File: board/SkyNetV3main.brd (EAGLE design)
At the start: 38 x 67 mm, 61 parts, among them IC1 HC_05, IC2 RF4463PRO, IC3 LPC1769, IC4 BCX17, IC5 TPS63001, IC6 MCP73871-2CCI/ML, Q1 32.768KHz, Q2 12MHz, Q3 IRLM6402, Q4 BSS138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

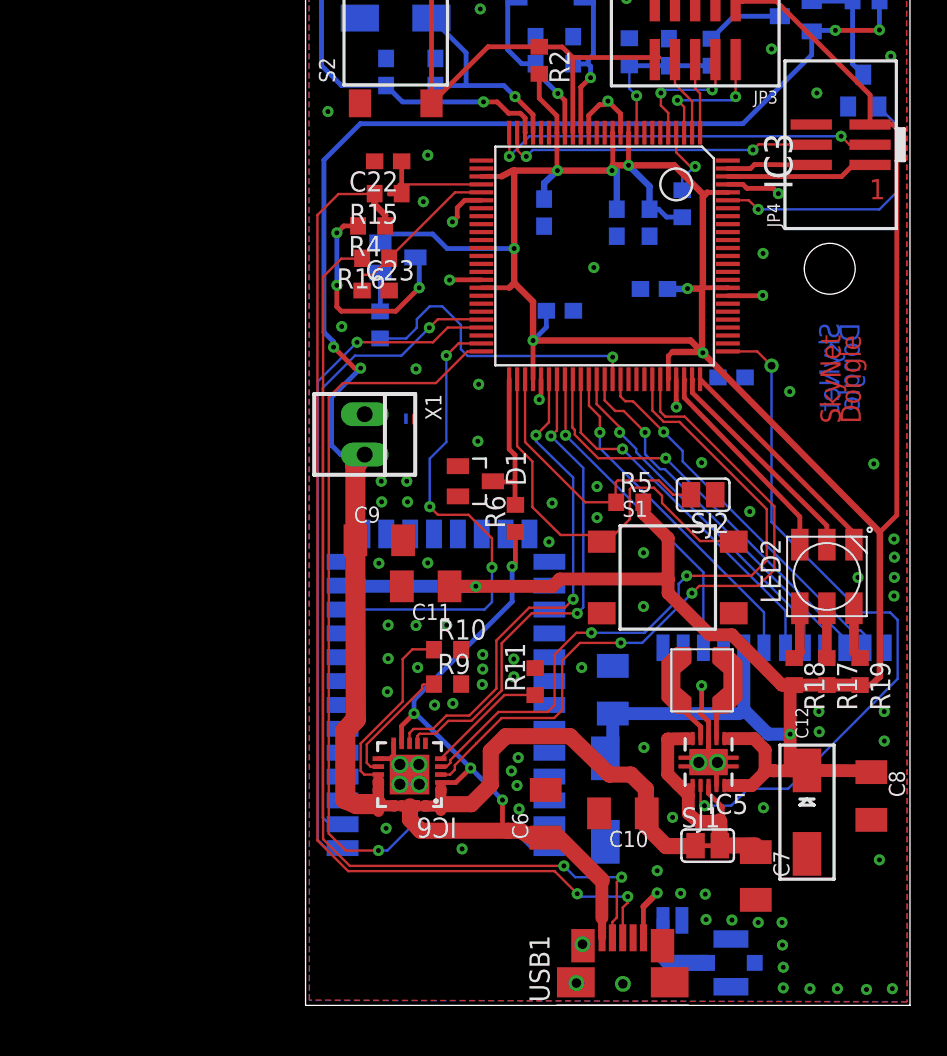
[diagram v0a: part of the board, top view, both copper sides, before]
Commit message: Schematic revised. TODO Radio remains
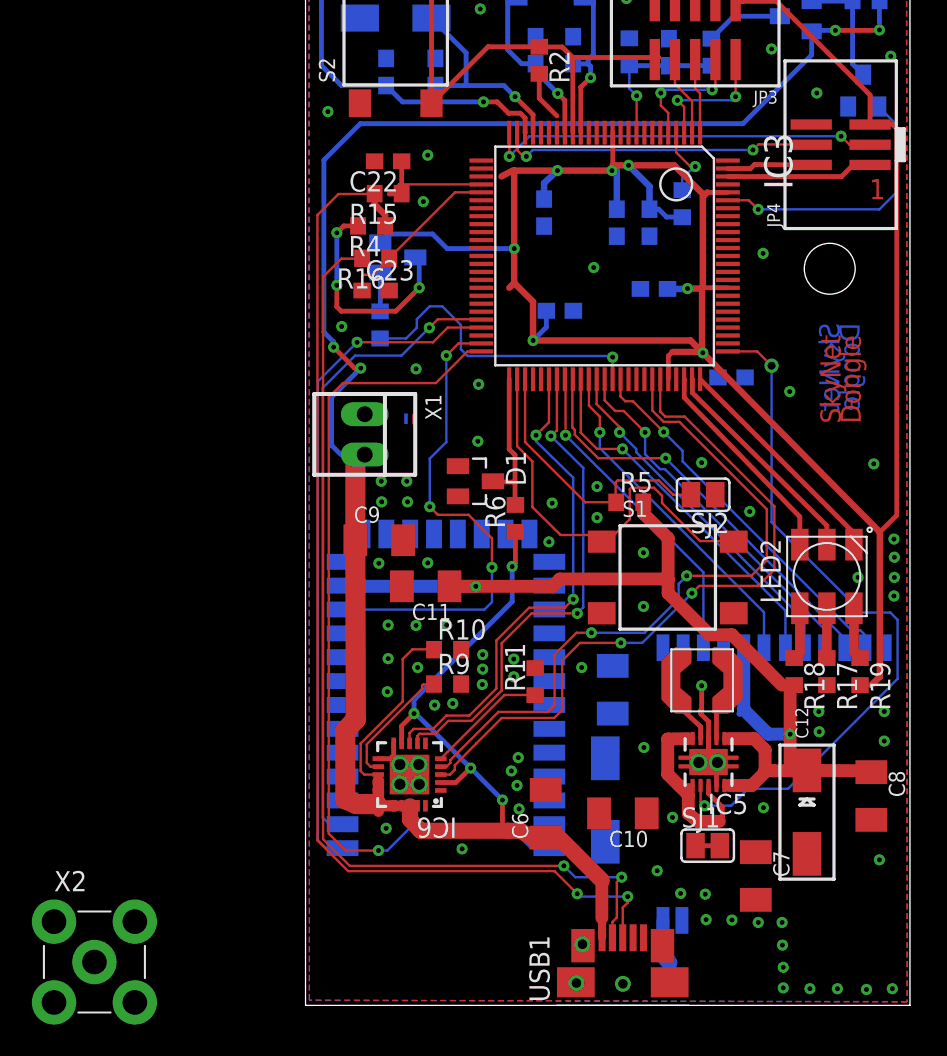
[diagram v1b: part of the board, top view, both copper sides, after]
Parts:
- removed U$1: ANT-MML, skynet_other:MML-2.0
- added X2: CONN-SMATHD, SteveMarple:SMA-THD
- R3: value 50 -> 1k
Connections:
- removed net OUT2: C10.1, IC6.1, IC6.20, SJ1.1
- new net BT-CN: IC1.32, IC3.48
- new net N$2: SJ1.1, X1.2
- net ANT: now also X2.SIG; no longer U$1.ANT
- net GND: now also IC1.21, IC1.22, X2.GND@0, X2.GND@1, X2.GND@2, X2.GND@3; no longer U$1.GND$1, U$1.GND$2, U$1.GND$3
- net V+: now also SJ1.2; no longer X1.2
- net VCC: now also C10.1, IC6.1, IC6.20; no longer SJ1.2
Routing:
- net OUT2: track 28.1 -> 0.00 mm
- net +3V3: track 244.3 -> 217.2 mm
- net GND: track 33.1 -> 11.5 mm, vias 96 -> 88
- net VCC: track 16.7 -> 13.0 mm
- net V+: track 93.7 -> 91.3 mm
- net ANT: track 5.19 -> 2.82 mm

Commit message: Schematic revised
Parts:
- removed X1: BAT, con-molex:22-23-2021
- added B1: PL503465, i7:PL503465
- added C14, C24: 10u, rcl:C1206K
- added Q5, Q6: IRLM6402, microbuilder:SOT23-WIDE
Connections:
- new net /BT-ON: IC3.32
- new net /RF-ON: IC3.33
- new net N$3: Q5.1
- new net N$4: Q6.1
- new net VDD: C11.1, IC1.12, Q5.3
- new net VEE: C1.1, C13.+, IC2.VCC, Q6.3
- net +3V3: now also C14.1, Q5.2, Q6.2; no longer C1.1, C11.1, C13.+, IC1.12, IC2.VCC
- net GND: now also B1.P-, C14.2, C24.2; no longer X1.1
- net N$2: now also B1.P+; no longer X1.2
- net VCC: now also C24.1
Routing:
- net +3V3: track 217.2 -> 210.9 mm
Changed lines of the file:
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@@
 <layer number="56" name="wert" color="7" fill="1" visible="no" active="no"/>
 <layer number="57" name="tCAD" color="7" fill="1" visible="no" active="no"/>
+<layer number="90" name="Modules" color="5" fill="1" visible="no" active="no"/>
 <layer number="91" name="Nets" color="2" fill="1" visible="no" active="no"/>
 <layer number="92" name="Busses" color="1" fill="1" visible="no" active="no"/>
@@
 <element name="L1" library="skynet_other" package="LPS4012" value="2u2" x="25.8064" y="21.5646"/>
 <element name="Q4" library="microbuilder" package="SOT23-WIDE" value="BSS138" x="35.8648" y="58.4708" rot="MR0"/>
-<element name="X1" library="con-molex" package="22-23-2021" value="BAT" x="4.5212" y="36.8554" rot="R270">
-<attribute name="OC_NEWARK" value="25C3832" x="-32.3088" y="-2.5146" size="1.778" layer="27" rot="R270" display="off"/>
-<attribute name="MPN" value="22-23-2021" x="-32.3088" y="-2.5146" size="1.778" layer="27" rot="R270" display="off"/>
-<attribute name="MF" value="MOLEX" x="-32.3088" y="-2.5146" size="1.778" layer="27" rot="R270" display="off"/>
-<attribute name="OC_FARNELL" value="1462926" x="-32.3088" y="-2.5146" size="1.778" layer="27" rot="R270" display="off"/>
-</element>
 <element name="USB1" library="usb_con-update" package="MOLEX-47364-0001" value="MOLEX-47346-0001" x="20.7442" y="2.4088" rot="R90"/>
 <element name="R15" library="rcl" package="R0603" value="33" x="5.9944" y="51.9938" rot="R180"/>
@@
 <element name="JP4" library="skynet_other" package="PIN-HEAD-1X3-SMD" value="EXT" x="34.4424" y="55.0672" rot="R90"/>
 <element name="X2" library="SteveMarple" package="SMA-THD" value="CONN-SMATHD" x="-12.4714" y="3.683"/>
+<element name="Q5" library="microbuilder" package="SOT23-WIDE" value="IRLM6402" x="-14.732" y="-2.1082"/>
+<element name="Q6" library="microbuilder" package="SOT23-WIDE" value="IRLM6402" x="-14.732" y="-5.588"/>
+<element name="C14" library="rcl" package="C1206K" value="10u" x="-14.1478" y="-9.8044"/>
+<element name="C24" library="rcl" package="C1206K" value="10u" x="-14.1478" y="-14.8844"/>
+<element name="B1" library="i7" package="PL503465" value="PL503465" x="-34.0868" y="-17.4244"/>
 </elements>
 <signals>
@@
 <contactref element="JP3" pad="5"/>
 <contactref element="JP3" pad="9"/>
-<contactref element="X1" pad="1"/>
 <contactref element="SJ2" pad="1"/>
 <contactref element="S1" pad="3"/>
@@
 <contactref element="C22" pad="2"/>
 <contactref element="C23" pad="2"/>
+<contactref element="C24" pad="2"/>
+<contactref element="C14" pad="2"/>
+<contactref element="B1" pad="P-"/>
 <wire x1="37.592" y1="60.6298" x2="36.9824" y2="66.3702" width="0" layer="19" extent="1-1"/>
 <wire x1="34.9148" y1="57.4708" x2="37.592" y2="60.6298" width="0" layer="19" extent="16-16"/>
@@
 <wire x1="32.3266" y1="10.481" x2="29.591" y2="13.3858" width="0" layer="19" extent="1-1"/>
 <wire x1="7.747" y1="40.9702" x2="11.684" y2="40.005" width="0" layer="19" extent="1-1"/>
-<wire x1="4.5212" y1="38.1254" x2="7.747" y2="40.9702" width="0" layer="19" extent="1-1"/>
 <wire x1="10.6426" y1="10.795" x2="14.224" y2="13.3096" width="0" layer="19" extent="1-1"/>
 <wire x1="36.3728" y1="12.6224" x2="32.3266" y2="10.481" width="0" layer="19" extent="1-1"/>
@@
 <wire x1="-15.0114" y1="1.143" x2="-15.0114" y2="6.223" width="0" layer="19" extent="1-1"/>
 <wire x1="-9.9314" y1="1.143" x2="-9.9314" y2="6.223" width="0" layer="19" extent="1-1"/>
+<wire x1="-12.6478" y1="-9.8044" x2="-15.0114" y2="1.143" width="0" layer="19" extent="1-1"/>
+<wire x1="-12.6478" y1="-14.8844" x2="-12.6478" y2="-9.8044" width="0" layer="19" extent="1-1"/>
+<wire x1="-42.5868" y1="-14.9244" x2="-12.6478" y2="-14.8844" width="0" layer="19" extent="1-16"/>
 </signal>
 <signal name="RTCX1">
@@
 </signal>
 <signal name="+3V3">
-<contactref element="IC1" pad="12"/>
 <contactref element="R2" pad="2"/>
-<contactref element="IC2" pad="VCC"/>
 <contactref element="R5" pad="2"/>
 <contactref element="IC5" pad="1"/>
@@
 <contactref element="C16" pad="1"/>
 <contactref element="C17" pad="1"/>
-<contactref element="C11" pad="1"/>
 <contactref element="JP3" pad="1"/>
 <contactref element="IC4" pad="2"/>
 <contactref element="R1" pad="2"/>
 <contactref element="C12" pad="+"/>
-<contactref element="C13" pad="+"/>
 <contactref element="JP4" pad="5"/>
 <wire x1="27.1366" y1="14.781" x2="27.3558" y2="14.781" width="0.3048" layer="1"/>
@@
 <wire x1="22.0472" y1="31.877" x2="22.0472" y2="32.727" width="0.8128" layer="1"/>
 <wire x1="22.0472" y1="32.727" x2="22.0336" y2="32.5882" width="0.8128" layer="1"/>
-<wire x1="9.8566" y1="27.305" x2="11.5062" y2="27.305" width="0.8128" layer="1"/>
 <via x="11.5062" y="27.305" extent="1-16" drill="0.3048"/>
 <wire x1="11.5062" y1="27.305" x2="3.1678" y2="27.305" width="0.8128" layer="16"/>
-<wire x1="3.1678" y1="27.305" x2="3.1282" y2="27.3446" width="0.8128" layer="16"/>
 <wire x1="11.5062" y1="27.305" x2="16.3322" y2="27.305" width="0.8128" layer="1"/>
 <wire x1="16.3322" y1="27.305" x2="16.7894" y2="27.7622" width="0.8128" layer="1"/>
@@
 <wire x1="27.6098" y1="24.257" x2="26.2128" y2="24.257" width="0.8128" layer="1"/>
 <wire x1="26.2128" y1="24.257" x2="23.5966" y2="26.8732" width="0.8128" layer="1"/>
-<wire x1="28.353" y1="23.444775" x2="28.353" y2="19.5646" width="0.8128" layer="16"/>
 <wire x1="28.353" y1="19.5646" x2="28.3464" y2="19.558" width="0.4064" layer="16"/>
 <wire x1="28.3464" y1="19.558" x2="29.8958" y2="18.0086" width="0.8128" layer="16"/>
 <wire x1="29.8958" y1="18.0086" x2="31.2674" y2="18.0086" width="0.8128" layer="16"/>
 <wire x1="28.091" y1="19.3026" x2="28.3464" y2="19.558" width="0.4064" layer="16"/>
-<wire x1="19.64865" y1="16.493" x2="20.1168" y2="16.96115" width="0.8128" layer="16"/>
 <contactref element="IC3" pad="10"/>
 <contactref element="IC3" pad="19"/>
@@
 <contactref element="IC3" pad="12"/>
 <contactref element="IC3" pad="71"/>
-<contactref element="C1" pad="1"/>
 <contactref element="R17" pad="2"/>
 <contactref element="R19" pad="2"/>
 <contactref element="R18" pad="2"/>
+<contactref element="Q6" pad="2"/>
+<contactref element="Q5" pad="2"/>
+<contactref element="C14" pad="1"/>
 <wire x1="27.352" y1="52.07" x2="27.3552" y2="52.0732" width="0" layer="19" extent="1-1"/>
 <wire x1="27.3552" y1="46.0732" x2="27.3528" y2="46.0756" width="0" layer="19" extent="1-1"/>
@@
 <wire x1="16.6052" y1="56.877" x2="16.6052" y2="55.8232" width="0" layer="19" extent="1-1"/>
 <wire x1="15.1052" y1="40.3232" x2="15.1052" y2="42.758371875" width="0" layer="19" extent="1-1"/>
-<wire x1="20.1168" y1="16.96115" x2="27.1366" y2="17.731" width="0" layer="19" extent="1-16"/>
-<wire x1="20.1168" y1="19.3026" x2="20.1168" y2="16.96115" width="0" layer="19" extent="16-16"/>
+<wire x1="-13.782" y1="-3.1082" x2="3.1678" y2="27.305" width="0" layer="19" extent="1-16"/>
+<wire x1="-13.782" y1="-6.588" x2="-13.782" y2="-3.1082" width="0" layer="19" extent="1-1"/>
+<wire x1="-15.6478" y1="-9.8044" x2="-13.782" y2="-6.588" width="0" layer="19" extent="1-1"/>
 </signal>
 <signal name="USB-CON-TRANS-2">
@@
 <contactref element="IC6" pad="20"/>
 <contactref element="C10" pad="1"/>
+<contactref element="C24" pad="1"/>
 <wire x1="26.8192" y1="12.5254" x2="29.0824" y2="11.0256" width="0" layer="19" extent="1-1"/>
 <wire x1="22.2518" y1="13.0302" x2="24.8666" y2="13.0302" width="0" layer="19" extent="1-1"/>
 <wire x1="9.3042" y1="14.4694" x2="22.2518" y2="13.0302" width="0" layer="19" extent="1-1"/>
 <wire x1="8.3392" y1="13.5044" x2="9.3042" y2="14.4694" width="0" layer="19" extent="1-1"/>
+<wire x1="-15.6478" y1="-14.8844" x2="8.3392" y2="13.5044" width="0" layer="19" extent="1-1"/>
 </signal>
 <signal name="V+">
@@
 </signal>
 <signal name="N$2">
-<contactref element="X1" pad="2"/>
 <contactref element="SJ1" pad="1"/>
-<wire x1="25.3206" y1="11.0002" x2="4.5212" y2="35.5854" width="0" layer="19" extent="1-1"/>
+<contactref element="B1" pad="P+"/>
+<wire x1="25.3206" y1="11.0002" x2="-25.5868" y2="-14.9244" width="0" layer="19" extent="1-16"/>
+</signal>
+<signal name="VEE">
+<contactref element="C13" pad="+"/>
+<contactref element="C1" pad="1"/>
+<contactref element="IC2" pad="VCC"/>
+<contactref element="Q6" pad="3"/>
+<wire x1="20.1168" y1="19.3026" x2="28.353" y2="23.444775" width="0" layer="19" extent="16-16"/>
+<wire x1="19.64865" y1="16.493" x2="20.1168" y2="19.3026" width="0" layer="19" extent="16-16"/>
+<wire x1="-14.732" y1="-4.588" x2="19.64865" y2="16.493" width="0" layer="19" extent="1-16"/>
+</signal>
+<signal name="VDD">
+<contactref element="C11" pad="1"/>
+<contactref element="IC1" pad="12"/>
+<contactref element="Q5" pad="3"/>
+<wire x1="3.1282" y1="27.3446" x2="9.8566" y2="27.305" width="0" layer="19" extent="1-16"/>
+<wire x1="-14.732" y1="-1.1082" x2="3.1282" y2="27.3446" width="0" layer="19" extent="1-16"/>
+</signal>
+<signal name="N$3">
+<contactref element="Q5" pad="1"/>
+</signal>
+<signal name="N$4">
+<contactref element="Q6" pad="1"/>
+</signal>
+<signal name="/RF-ON">
+<contactref element="IC3" pad="33"/>
+</signal>
+<signal name="/BT-ON">
+<contactref element="IC3" pad="32"/>
 </signal>
 </signals>

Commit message: psu done
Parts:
- moved Q5 123.8 mm to (108.0, 14.7)
- moved B1 68.2 mm to (31.6, 0.97), flipped to the bottom
- moved C14 65.2 mm to (44.8, 18.1)
- moved C24 63.7 mm to (44.8, 9.23)
- moved Q6 60.0 mm to (39.7, 19.6), turned to 90 degrees
- moved JP4 51.9 mm to (86.3, 57.8)
- moved R12 51.9 mm to (78.2, 63.6)
- moved R13 51.9 mm to (73.0, 63.6)
- moved R14 51.9 mm to (87.9, 66.8)
- moved R19 51.9 mm to (87.5, 24.6)
- moved S2 51.9 mm to (58.3, 64.5)
- moved C11 51.9 mm to (60.2, 30.0)
- moved C15 51.9 mm to (75.5, 63.6)
- moved C16 51.9 mm to (74.6, 48.7)
- moved C18 51.9 mm to (72.2, 52.9)
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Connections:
- removed net N$3: Q5.1
- removed net N$4: Q6.1
- net /BT-ON: now also Q5.1
- net /RF-ON: now also Q6.1
- net GND: now also IC5.TH
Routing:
- net +3V3: track 210.9 -> 19.3 mm, vias 9 -> 2
- net GND: track 11.5 -> 141.8 mm, vias 88 -> 16
- net V+: track 91.3 -> 13.9 mm, vias 4 -> 0
- net BT-AT: track 54.0 -> 0.00 mm, vias 1 -> 0
- net USB-CABLE-D+: track 69.5 -> 17.5 mm, vias 2 -> 0
- net USB-CABLE-D-: track 62.1 -> 17.8 mm, vias 2 -> 0
- net BT-TX: track 42.3 -> 0.00 mm, vias 1 -> 0
- net BT-RX: track 40.2 -> 0.00 mm, vias 1 -> 0
- net DCDCPS: track 43.9 -> 12.7 mm, vias 2 -> 1
- net BT-RESET: track 30.8 -> 0.00 mm, vias 3 -> 0
- net RESET: track 29.3 -> 0.00 mm
- net INPUT: track 28.3 -> 0.00 mm
- net RF-NIRQ: track 26.4 -> 0.00 mm, vias 1 -> 0
- net SDA-EXT: track 24.9 -> 0.00 mm, vias 2 -> 0
- net CHGSEL-L: track 43.3 -> 19.1 mm, vias 2 -> 1
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- added copper zone on layer 16, net N$5
- removed copper zone on layer 16, net GND
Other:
- board size 38 x 67 mm -> 47.4 x 67 mm
- board text removed: "-"
- board text removed: "1"
- board text removed: "SkyNet Dongle"

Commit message: cpu moved
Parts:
- moved Q5 101.6 mm to (16.6, 59.1)
- moved R19 85.3 mm to (12.8, 65.7), turned to 0 degrees
- moved R17 82.5 mm to (12.8, 63.7), turned to 0 degrees
- moved R18 79.7 mm to (12.8, 61.6), turned to 0 degrees
- moved S1 72.1 mm to (8.38, 56.9), turned to 180 degrees
- moved SJ2 62.3 mm to (15.9, 27.1), turned to 270 degrees
- moved C11 55.0 mm to (16.7, 63.7), turned to 270 degrees
- moved R5 54.0 mm to (19.4, 28.9)
- moved R14 51.9 mm to (47.9, 33.7), flipped to the top, turned to 270 degrees
- moved Q4 50.9 mm to (47.3, 30.4), flipped to the top, turned to 270 degrees
- moved Q3 50.0 mm to (45.2, 33.7), flipped to the top, turned to 90 degrees
- moved R6 47.8 mm to (19.3, 23.6), turned to 0 degrees
- moved R12 46.7 mm to (42.6, 33.4), flipped to the top
- moved JP3 45.7 mm to (36.3, 44.6), turned to 270 degrees
- moved D1 45.5 mm to (19.1, 26.3)
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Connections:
- net /BT-ON: now also IC3.95; no longer IC3.32
- net /RF-ON: now also IC3.76; no longer IC3.33
- net AD-PWR: now also IC3.86; no longer IC3.95
- net DCDCPS: now also IC3.77; no longer IC3.76
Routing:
- net V+: track 13.9 -> 63.3 mm, vias 0 -> 2
- net GND: track 141.8 -> 171.1 mm, vias 16 -> 22
- net USB-CABLE-D+: track 17.5 -> 40.8 mm, vias 0 -> 1
- net +5V: track 34.1 -> 57.0 mm, vias 5 -> 6
- net USB-CABLE-D-: track 17.8 -> 38.8 mm, vias 0 -> 1
- net RF-GPIO0: track 0.00 -> 16.7 mm
- net PROG: track 0.00 -> 16.6 mm
- net +3V3: track 19.3 -> 32.4 mm
- net RF-SDO: track 0.00 -> 12.7 mm
- net RF-SDI: track 0.00 -> 11.4 mm, vias 0 -> 2
- net RF-SCLK: track 0.00 -> 10.5 mm
- net DCDCPS: track 12.7 -> 22.7 mm, vias 1 -> 2
- net CHG-S1: track 14.2 -> 22.9 mm, vias 1 -> 2
- net AD-PWR: track 0.00 -> 8.64 mm
- net RF-NSEL: track 0.00 -> 8.59 mm
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- added copper zone on layer 16, net GND
- removed copper zone on layer 16, net N$5
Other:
- board text added: "bt anderer uart"
- board text added: "kleinerer reset taster"
- board text added: "led anderer pwm"

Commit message: pre-molex-connector
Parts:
- added X1: 52745-1290, con-molex:52745-1290
- 1K: value 1k -> 330
- moved C18 56.0 mm to (16.3, 55.8), flipped to the top, turned to 0 degrees
- moved C21 53.3 mm to (19.5, 30.6), flipped to the top, turned to 180 degrees
- moved R2 16.1 mm to (40.5, 32.1), turned to 270 degrees
- moved S2 13.7 mm to (44.3, 36.9)
- moved JP4 2.35 mm to (43.5, 45.6)
- moved Q3 2.11 mm to (45.2, 31.6)
- moved C15 2.11 mm to (44.6, 28.3)
- moved Q4 2.11 mm to (47.3, 28.3)
- moved R12 2.11 mm to (42.6, 31.3)
- moved R13 2.11 mm to (42.6, 28.3)
- moved R14 2.11 mm to (47.9, 31.6)
- moved Q2 1.60 mm to (20.7, 46.1)
- moved JP3 1.46 mm to (35.3, 45.6)
- moved C11 1.27 mm to (16.9, 64.9)
- moved C2 1.14 mm to (29.4, 42.7)
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- renumbered R3 to 1K
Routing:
- net GND: track 171.1 -> 343.8 mm, vias 22 -> 27
- net +3V3: track 32.4 -> 153.7 mm, vias 2 -> 6
- net VDD: track 0.00 -> 17.3 mm
- net XTAL1: track 0.00 -> 11.4 mm
- net XTAL2: track 0.00 -> 10.4 mm
- net RESET: track 0.00 -> 10.1 mm
- net RTCX2: track 0.00 -> 7.65 mm
- net RTCX1: track 0.00 -> 6.50 mm
- net /BT-ON: track 0.00 -> 5.35 mm
- net AD-PWR: track 8.64 -> 13.5 mm
- net AD-IN: track 3.33 -> 6.50 mm, vias 0 -> 1
- net LED-B-R: track 0.00 -> 1.92 mm
- net LED-G-R: track 0.00 -> 1.92 mm
- net LED-R-R: track 0.00 -> 1.78 mm
- net V+: track 63.3 -> 64.7 mm
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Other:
- board text added: "q2: 2 freie pins"

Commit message: cleanup after routing
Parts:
- removed JP3: JTAG, microbuilder:2X05_1.27MM_SMT
- removed JP4: EXT, skynet_other:PIN-HEAD-1X3-SMD
- removed X1: 52745-1290, con-molex:52745-1290
- added S3: (no value), sid:MOLEX-52892-1233
- added TP1, TP2: PTR1B1,27, testpad:B1,27
- moved C19 45.8 mm to (29.5, 43.2), flipped to the top, turned to 90 degrees
- moved R1 32.9 mm to (45.8, 41.9), flipped to the top
- moved C16 31.5 mm to (43.8, 41.9), flipped to the top, turned to 90 degrees
- moved C2 1.95 mm to (27.5, 43.2), turned to 90 degrees
- moved Q1 1.56 mm to (27.3, 46.2)
- moved C3 1.05 mm to (25.5, 43.2), turned to 90 degrees
- moved IC4 0.69 mm to (16.3, 39.9)
- moved R4 0.60 mm to (16.9, 36.6)
- moved C5 0.38 mm to (19.5, 42.7)
- moved Q2 0.38 mm to (20.3, 46.1)
- moved C4 0.38 mm to (22.8, 42.7)
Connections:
- new net AD-EXT: IC3.6, S3.P$11
- net +3V3: now also S3.P$1; no longer JP3.1, JP4.5
- net /BT-ON: now also IC3.26; no longer IC3.95
- net BT-AT: now also IC3.7; no longer IC3.50
- net BT-CN: now also IC3.8; no longer IC3.48
- net BT-RESET: now also IC3.27; no longer IC3.49
- net GND: now also S3.P$12, S3.P$GND1, S3.P$GND2; no longer JP3.3, JP3.5, JP3.9, JP4.6
- net JTAG_TCK: now also S3.P$10; no longer JP3.4
- net JTAG_TDI: now also S3.P$8; no longer JP3.8
- net JTAG_TDO: now also S3.P$7; no longer JP3.6
- net JTAG_TMS: now also S3.P$9; no longer JP3.2
- net LED-B: now also IC3.32; no longer IC3.75
- net LED-G: now also IC3.35; no longer IC3.73
- net LED-R: now also IC3.34; no longer IC3.74
- net RESET: now also S3.P$4; no longer JP3.10
- net RX: now also S3.P$5, TP2.TP; no longer JP4.2
- net SCL-EXT: now also S3.P$3; no longer JP4.4
- net SDA-EXT: now also S3.P$2; no longer JP4.3
- net TX: now also S3.P$6, TP1.TP; no longer JP4.1
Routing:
- net GND: track 343.8 -> 452.2 mm, vias 27 -> 75
- net +3V3: track 153.7 -> 227.8 mm, vias 6 -> 8
- net BT-TX: track 0.00 -> 61.9 mm, vias 0 -> 2
- net BT-RX: track 0.00 -> 59.1 mm, vias 0 -> 2
- net INPUT: track 0.00 -> 46.3 mm, vias 0 -> 2
- net LED-B: track 0.00 -> 46.0 mm, vias 0 -> 2
- net LED-R: track 0.00 -> 45.2 mm, vias 0 -> 2
- net LED-G: track 0.00 -> 44.2 mm, vias 0 -> 2
- net BT-RESET: track 0.00 -> 30.2 mm, vias 0 -> 2
- net USB-CON: track 0.00 -> 23.7 mm, vias 0 -> 2
- net /BT-ON: track 5.35 -> 27.6 mm
- net RESET: track 10.1 -> 29.9 mm, vias 0 -> 2
- net SCL-EXT: track 0.00 -> 19.4 mm, vias 0 -> 2
- net SDA-EXT: track 0.00 -> 18.9 mm, vias 0 -> 2
- net JTAG-TRST: track 0.00 -> 17.2 mm, vias 0 -> 2
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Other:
- board text added: "+"
- board text added: "SkyNet v3.1 i7"
- board text removed: "bt anderer uart"
- board text removed: "kleinerer reset taster"
- board text removed: "led anderer pwm"
